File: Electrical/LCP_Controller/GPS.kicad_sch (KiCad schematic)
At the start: 12 parts, among them J12 SALEAE_TEST, J34 Conn_01x04, Q10 TSM500P02CX RFG, U13 MAX-M8Q

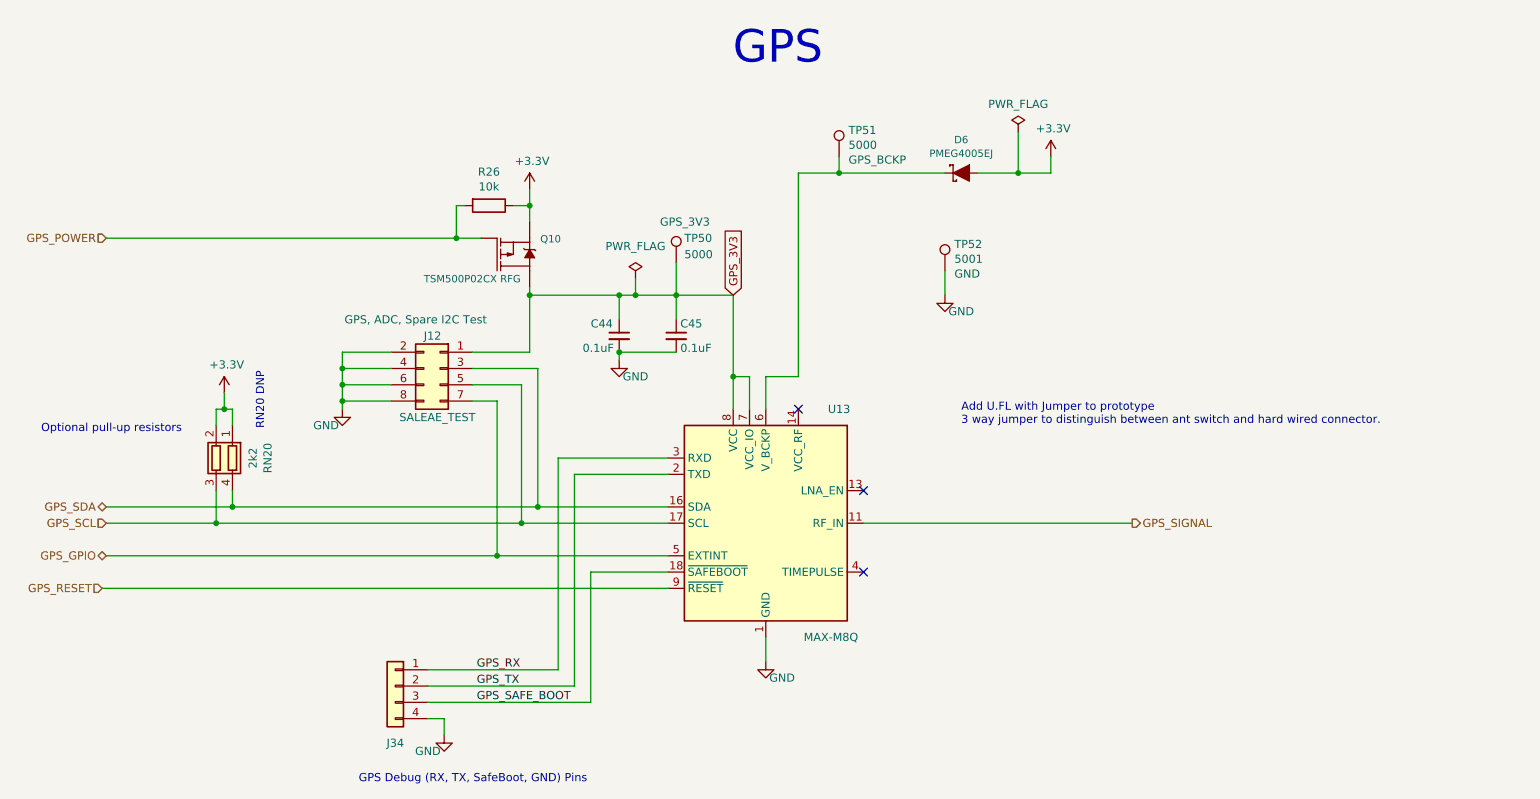
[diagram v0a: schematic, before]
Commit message: Hardware Revision : v0.3
1. modified schematic design, removed unnecessary test points.
2. pcb layout 2x8 Inches allowance dimension, layout is in progress
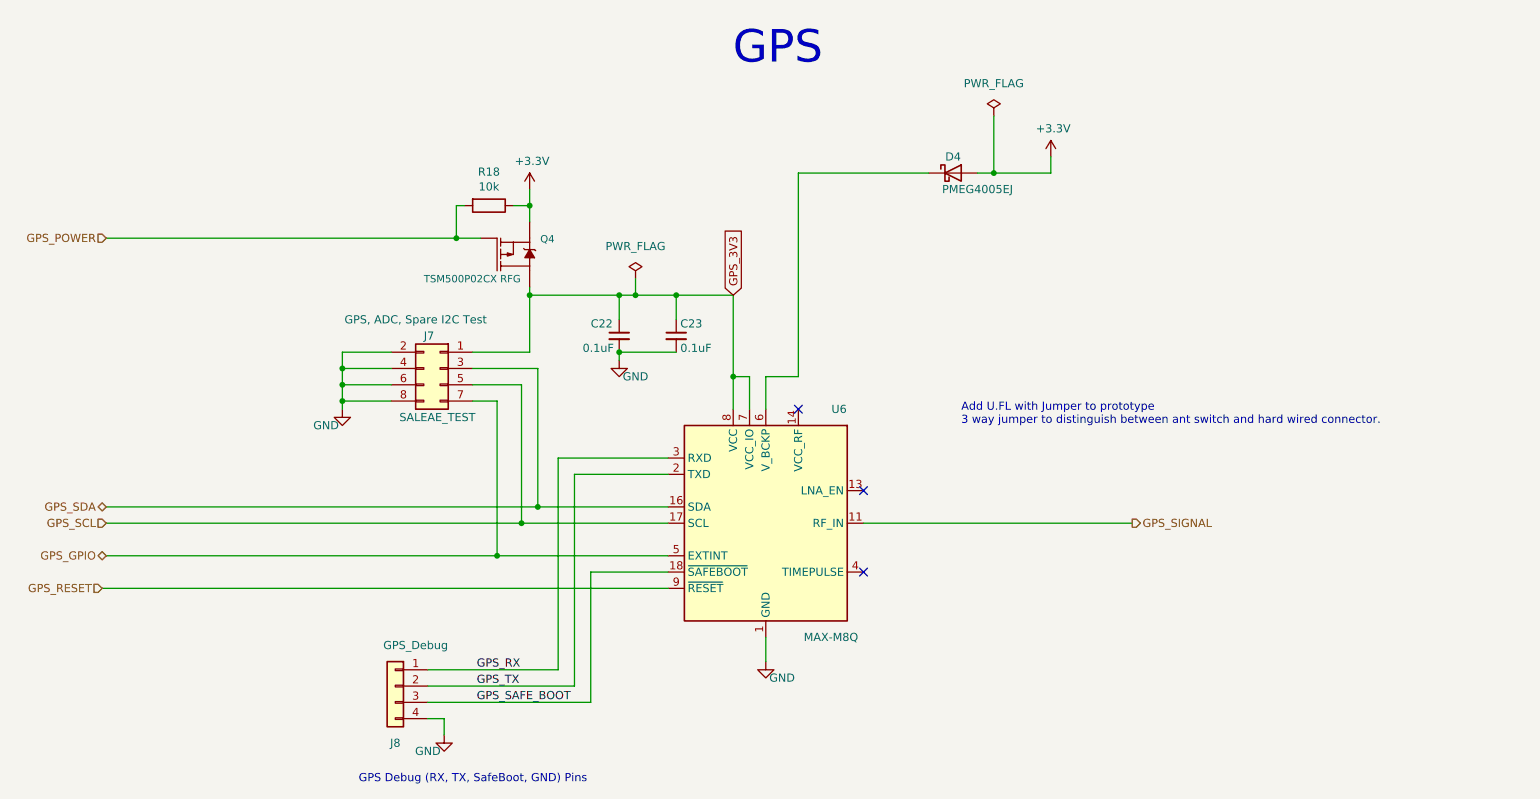
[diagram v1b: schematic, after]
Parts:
- removed D6: PMEG4005EJ, Diode_SMD:D_SOD-323F, symbol SparkFun-DiscreteSemi:DIODE-SCHOTTKY-PMEG4005EJ
- removed RN20: 2k2, Resistor_SMD:R_Array_Concave_2x0603, symbol Device:R_Pack02
- removed TP50, TP51: 5000, TestPoint:TestPoint_Keystone_5000-5004_Miniature, symbol Connector:TestPoint
- removed TP52: 5001, TestPoint:TestPoint_Keystone_5000-5004_Miniature, symbol Connector:TestPoint
- added D4: PMEG4005EJ, Diode_SMD:D_SOD-323, symbol Device:D_Schottky
- J8: renamed from J34; value Conn_01x04 -> GPS_Debug
- renumbered C44 to C22, C45 to C23, J12 to J7, Q10 to Q4, R26 to R18, U13 to U6
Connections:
- net +3.3V: now also D4.2 (A)
- net at U6.6 (V_BCKP): now also D4.1 (K)
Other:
- note removed: "Optional pull-up resistors"
- note removed: "RN20 DNP"

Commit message: Hw Rev : 0.3v
changed buck-coverter LMR50410XDBVR to BD9G102G-LB, added schotty diode.
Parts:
- D4: value PMEG4005EJ -> RB400VAM-50TR; MPN PMEG4005EJ -> RB400VAM-50TR
- U6: MPN (none) -> MAX-8C-0
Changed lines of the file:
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@@
+      (effects (font (size 1.27 1.27)) hide)
+    )
+    (property "MPN" "MAX-8C-0" (id 4) (at 161.29 106.68 0)
       (effects (font (size 1.27 1.27)) hide)
     )
@@
     (in_bom yes) (on_board yes)
     (property "Reference" "D4" (id 0) (at 190.5 49.53 0))
-    (property "Value" "PMEG4005EJ" (id 1) (at 194.31 54.61 0))
+    (property "Value" "RB400VAM-50TR" (id 1) (at 194.31 54.61 0))
     (property "Footprint" "Diode_SMD:D_SOD-323" (id 2) (at 190.5 52.07 0)
       (effects (font (size 1.27 1.27)) hide)
@@
       (effects (font (size 1.27 1.27)) hide)
     )
-    (property "MPN" "PMEG4005EJ" (id 4) (at 190.5 52.07 0)
+    (property "MPN" "RB400VAM-50TR" (id 4) (at 190.5 52.07 0)
       (effects (font (size 1.27 1.27)) hide)
     )

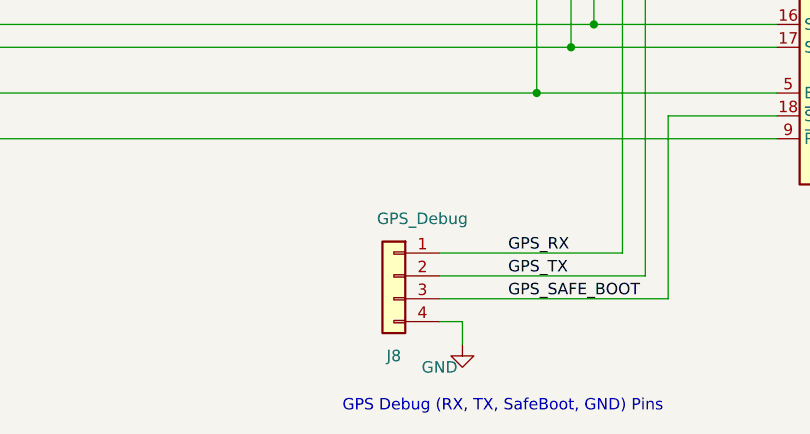
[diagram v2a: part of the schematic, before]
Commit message: Hw Rev : 0.3v updated
changed TRS3122ERGER to TRS3122ERGET due to shortage of part.
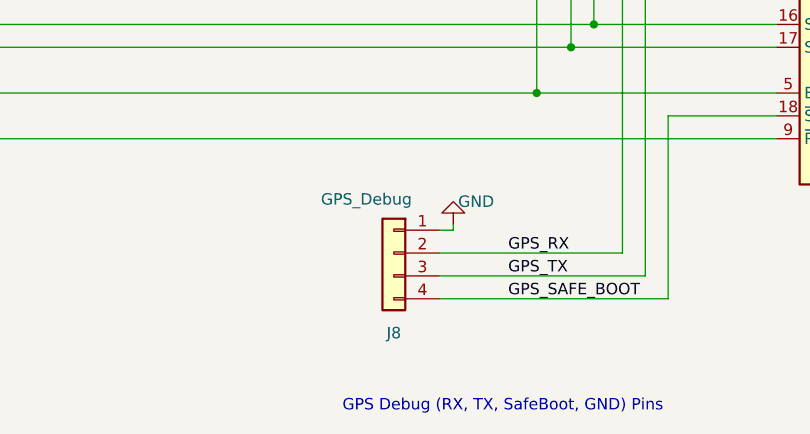
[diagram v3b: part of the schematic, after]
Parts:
- D4: footprint Diode_SMD:D_SOD-323 -> Diode_SMD:D_SOD-323F
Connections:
- net GND: now also J8.1 (Pin_1); no longer J8.4 (Pin_4)
- net GPS_RX: now also J8.2 (Pin_2); no longer J8.1 (Pin_1)
- net GPS_SAFE_BOOT: now also J8.4 (Pin_4); no longer J8.3 (Pin_3)
- net GPS_TX: now also J8.3 (Pin_3); no longer J8.2 (Pin_2)
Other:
- moved on the sheet: J8
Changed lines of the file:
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@@
-    (stroke (width 0) (type default) (color 0 0 0 0))
-  )
-  (wire (pts (xy 111.125 137.16) (xy 108.585 137.16))
     (stroke (width 0) (type default) (color 0 0 0 0))
   )
@@
     (stroke (width 0) (type default) (color 0 0 0 0))
   )
+  (wire (pts (xy 110.109 127) (xy 108.585 127))
+    (stroke (width 0) (type default) (color 0 0 0 0))
+  )
   (wire (pts (xy 113.03 57.15) (xy 114.3 57.15))
     (stroke (width 0) (type default) (color 0 0 0 0))
@@
     (stroke (width 0) (type default) (color 0 0 0 0))
   )
+  (wire (pts (xy 110.109 126.365) (xy 110.109 127))
+    (stroke (width 0) (type default) (color 0 0 0 0))
+  )
   (wire (pts (xy 146.05 96.52) (xy 128.905 96.52))
     (stroke (width 0) (type default) (color 0 0 0 0))
   )
   (wire (pts (xy 194.31 52.07) (xy 196.85 52.07))
-    (stroke (width 0) (type default) (color 0 0 0 0))
-  )
-  (wire (pts (xy 111.125 139.7) (xy 111.125 137.16))
     (stroke (width 0) (type default) (color 0 0 0 0))
   )
@@
     (property "Reference" "D4" (id 0) (at 190.5 49.53 0))
     (property "Value" "RB400VAM-50TR" (id 1) (at 194.31 54.61 0))
-    (property "Footprint" "Diode_SMD:D_SOD-323" (id 2) (at 190.5 52.07 0)
+    (property "Footprint" "Diode_SMD:D_SOD-323F" (id 2) (at 190.5 52.07 0)
       (effects (font (size 1.27 1.27)) hide)
     )
@@
     (pin "2")
   )
-  (symbol (lib_id "Connector_Generic:Conn_01x04") (at 103.505 132.08 0) (mirror y) (unit 1)
-    (in_bom yes) (on_board yes)
-    (property "Reference" "J8" (id 0) (at 103.505 140.97 0))
-    (property "Value" "GPS_Debug" (id 1) (at 106.68 125.73 0))
-    (property "Footprint" "Connector_PinHeader_2.54mm:PinHeader_1x04_P2.54mm_Vertical" (id 2) (at 103.505 132.08 0)
-      (effects (font (size 1.27 1.27)) hide)
-    )
-    (property "Datasheet" "~" (id 3) (at 103.505 132.08 0)
-      (effects (font (size 1.27 1.27)) hide)
-    )
-    (property "MPN" "" (id 4) (at 103.505 132.08 0)
+  (symbol (lib_id "Connector_Generic:Conn_01x04") (at 103.505 129.54 0) (mirror y) (unit 1)
+    (in_bom yes) (on_board yes)
+    (property "Reference" "J8" (id 0) (at 103.505 138.43 0))
+    (property "Value" "GPS_Debug" (id 1) (at 100.457 123.571 0))
+    (property "Footprint" "Connector_PinHeader_2.54mm:PinHeader_1x04_P2.54mm_Vertical" (id 2) (at 103.505 129.54 0)
+      (effects (font (size 1.27 1.27)) hide)
+    )
+    (property "Datasheet" "~" (id 3) (at 103.505 129.54 0)
+      (effects (font (size 1.27 1.27)) hide)
+    )
+    (property "MPN" "" (id 4) (at 103.505 129.54 0)
       (effects (font (size 1.27 1.27)) hide)
     )
@@
     (pin "4")
   )
-  (symbol (lib_id "power:GND") (at 111.125 139.7 0) (unit 1)
-    (in_bom yes) (on_board yes)
-    (property "Reference" "#PWR053" (id 0) (at 111.125 146.05 0)
-      (effects (font (size 1.27 1.27)) hide)
-    )
-    (property "Value" "GND" (id 1) (at 108.585 142.24 0))
-    (property "Footprint" "" (id 2) (at 111.125 139.7 0)
-      (effects (font (size 1.27 1.27)) hide)
-    )
-    (property "Datasheet" "" (id 3) (at 111.125 139.7 0)
-      (effects (font (size 1.27 1.27)) hide)
-    )
+  (symbol (lib_id "power:GND") (at 110.109 126.365 180) (unit 1)
+    (in_bom yes) (on_board yes)
+    (property "Reference" "#PWR053" (id 0) (at 110.109 120.015 0)
+      (effects (font (size 1.27 1.27)) hide)
+    )
+    (property "Value" "GND" (id 1) (at 112.649 123.825 0))
+    (property "Footprint" "" (id 2) (at 110.109 126.365 0)
+      (effects (font (size 1.27 1.27)) hide)
+    )
+    (property "Datasheet" "" (id 3) (at 110.109 126.365 0)
+      (effects (font (size 1.27 1.27)) hide)
+    )

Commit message: Hw Rev : 0.3v , update
changed package type D_SOD-323 to D_TUMD2 for D4,D7
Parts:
- D4: footprint Diode_SMD:D_SOD-323F -> Diode_SMD:D_TUMD2
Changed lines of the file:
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@@
     (property "Reference" "D4" (id 0) (at 190.5 49.53 0))
     (property "Value" "RB400VAM-50TR" (id 1) (at 194.31 54.61 0))
-    (property "Footprint" "Diode_SMD:D_SOD-323F" (id 2) (at 190.5 52.07 0)
+    (property "Footprint" "Diode_SMD:D_TUMD2" (id 2) (at 190.5 52.07 0)
       (effects (font (size 1.27 1.27)) hide)
     )

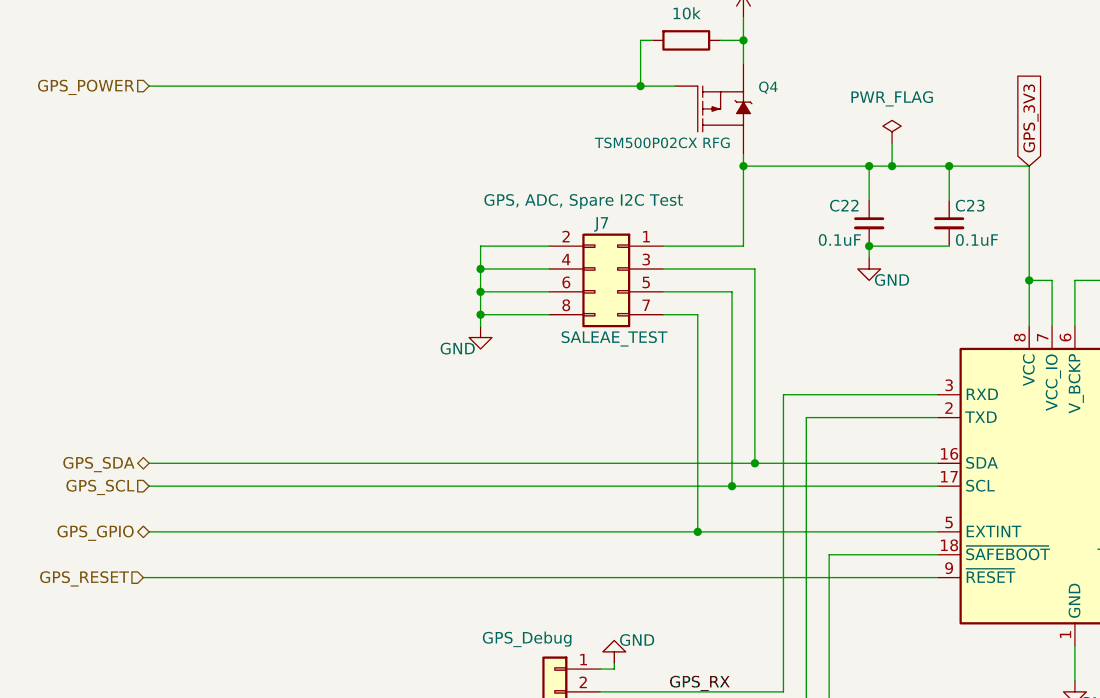
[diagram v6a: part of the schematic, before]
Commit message: New Layout
Changes for this Rev:
- Impedance Matched GPS traces
- Copper Pours
- Vias/Traces changed to bring down costs
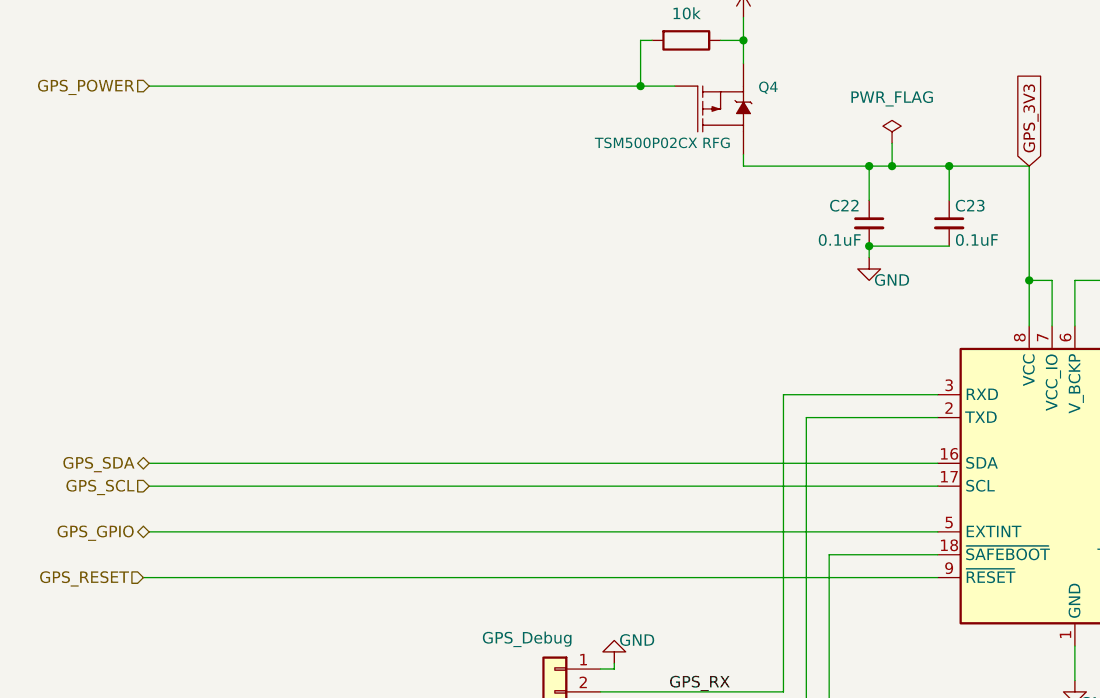
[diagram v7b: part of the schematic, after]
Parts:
- removed J7: SALEAE_TEST, Connector_PinHeader_2.54mm:PinHeader_2x04_P2.54mm_Vertical, symbol Connector_Generic:Conn_02x04_Odd_Even
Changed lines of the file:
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@@
     (comment 6 "Current Design Updated by: Joseph Kurina")
   )
-  (junction (at 119.38 111.76) (diameter 0) (color 0 0 0 0)
-  )
   (junction (at 140.97 71.12) (diameter 0) (color 0 0 0 0)
   )
-  (junction (at 95.25 87.63) (diameter 0) (color 0 0 0 0)
-  )
-  (junction (at 95.25 82.55) (diameter 0) (color 0 0 0 0)
-  )
   (junction (at 147.32 71.12) (diameter 0) (color 0 0 0 0)
-  )
-  (junction (at 125.73 104.14) (diameter 0) (color 0 0 0 0)
-  )
-  (junction (at 95.25 85.09) (diameter 0) (color 0 0 0 0)
-  )
-  (junction (at 124.46 71.12) (diameter 0) (color 0 0 0 0)
-  )
-  (junction (at 123.19 106.68) (diameter 0) (color 0 0 0 0)
   )
   (junction (at 138.43 71.12) (diameter 0) (color 0 0 0 0)
@@
     (stroke (width 0) (type default))
   )
-  (wire (pts (xy 119.38 87.63) (xy 119.38 111.76))
-    (stroke (width 0) (type default))
-  )
   (wire (pts (xy 138.43 80.01) (xy 147.32 80.01))
     (stroke (width 0) (type default))
   )
-  (wire (pts (xy 123.19 85.09) (xy 123.19 106.68))
-    (stroke (width 0) (type default))
-  )
   (wire (pts (xy 138.43 74.93) (xy 138.43 71.12))
     (stroke (width 0) (type default))
@@
     (stroke (width 0) (type default))
   )
-  (wire (pts (xy 58.42 106.68) (xy 123.19 106.68))
-    (stroke (width 0) (type default))
-  )
-  (wire (pts (xy 125.73 104.14) (xy 146.05 104.14))
+  (wire (pts (xy 58.42 104.14) (xy 146.05 104.14))
     (stroke (width 0) (type default))
   )
@@
     (stroke (width 0) (type default))
   )
-  (wire (pts (xy 95.25 82.55) (xy 95.25 85.09))
-    (stroke (width 0) (type default))
-  )
-  (wire (pts (xy 115.57 85.09) (xy 123.19 85.09))
-    (stroke (width 0) (type default))
-  )
-  (wire (pts (xy 102.87 85.09) (xy 95.25 85.09))
-    (stroke (width 0) (type default))
-  )
   (wire (pts (xy 147.32 74.93) (xy 147.32 71.12))
     (stroke (width 0) (type default))
@@
     (stroke (width 0) (type default))
   )
-  (wire (pts (xy 95.25 87.63) (xy 95.25 88.9))
-    (stroke (width 0) (type default))
-  )
-  (wire (pts (xy 115.57 80.01) (xy 124.46 80.01))
-    (stroke (width 0) (type default))
-  )
-  (wire (pts (xy 95.25 80.01) (xy 102.87 80.01))
-    (stroke (width 0) (type default))
-  )
-  (wire (pts (xy 102.87 82.55) (xy 95.25 82.55))
-    (stroke (width 0) (type default))
-  )
   (wire (pts (xy 156.21 71.12) (xy 156.21 83.82))
     (stroke (width 0) (type default))
@@
     (stroke (width 0) (type default))
   )
-  (wire (pts (xy 58.42 111.76) (xy 119.38 111.76))
-    (stroke (width 0) (type default))
-  )
   (wire (pts (xy 58.42 62.23) (xy 113.03 62.23))
     (stroke (width 0) (type default))
@@
     (stroke (width 0) (type default))
   )
-  (wire (pts (xy 115.57 82.55) (xy 125.73 82.55))
-    (stroke (width 0) (type default))
-  )
   (wire (pts (xy 116.84 62.23) (xy 113.03 62.23))
     (stroke (width 0) (type default))
   )
-  (wire (pts (xy 102.87 87.63) (xy 95.25 87.63))
-    (stroke (width 0) (type default))
-  )
   (wire (pts (xy 196.85 52.07) (xy 205.74 52.07))
     (stroke (width 0) (type default))
@@
     (stroke (width 0) (type default))
   )
-  (wire (pts (xy 119.38 111.76) (xy 146.05 111.76))
+  (wire (pts (xy 58.42 111.76) (xy 146.05 111.76))
     (stroke (width 0) (type default))
   )
@@
     (stroke (width 0) (type default))
   )
-  (wire (pts (xy 95.25 85.09) (xy 95.25 87.63))
-    (stroke (width 0) (type default))
-  )
   (wire (pts (xy 131.445 132.08) (xy 108.585 132.08))
     (stroke (width 0) (type default))
   )
-  (wire (pts (xy 95.25 82.55) (xy 95.25 80.01))
-    (stroke (width 0) (type default))
-  )
   (wire (pts (xy 133.985 134.62) (xy 108.585 134.62))
     (stroke (width 0) (type default))
@@
     (stroke (width 0) (type default))
   )
-  (wire (pts (xy 58.42 104.14) (xy 125.73 104.14))
-    (stroke (width 0) (type default))
-  )
   (wire (pts (xy 128.905 129.54) (xy 108.585 129.54))
     (stroke (width 0) (type default))
   )
-  (wire (pts (xy 115.57 87.63) (xy 119.38 87.63))
-    (stroke (width 0) (type default))
-  )
-  (wire (pts (xy 123.19 106.68) (xy 146.05 106.68))
+  (wire (pts (xy 58.42 106.68) (xy 146.05 106.68))
     (stroke (width 0) (type default))
   )
@@
   )
   (wire (pts (xy 158.75 83.82) (xy 158.75 88.9))
-    (stroke (width 0) (type default))
-  )
-  (wire (pts (xy 125.73 82.55) (xy 125.73 104.14))
-    (stroke (width 0) (type default))
-  )
-  (wire (pts (xy 124.46 71.12) (xy 124.46 80.01))
     (stroke (width 0) (type default))
   )
@@
     (effects (font (size 1.27 1.27)) (justify right))
   )
-  (symbol (lib_id "Connector_Generic:Conn_02x04_Odd_Even") (at 110.49 82.55 0) (mirror y) (unit 1)
-    (in_bom yes) (on_board yes) (dnp no)
-    (property "Reference" "J7" (at 107.95 77.47 0)
-      (effects (font (size 1.27 1.27)) (justify right))
-    )
-    (property "Value" "SALEAE_TEST" (at 104.14 90.17 0)
-      (effects (font (size 1.27 1.27)) (justify right))
-    )
-    (property "Footprint" "Connector_PinHeader_2.54mm:PinHeader_2x04_P2.54mm_Vertical" (at 110.49 82.55 0)
-      (effects (font (size 1.27 1.27)) hide)
-    )
-    (property "Datasheet" "~" (at 110.49 82.55 0)
-      (effects (font (size 1.27 1.27)) hide)
-    )
-    (property "TestPoint" "GPS, ADC, Spare I2C Test" (at 106.68 74.93 0)
-      (effects (font (size 1.27 1.27)))
-    )
-    (property "MPN" "0010897080" (at 110.49 82.55 0)
-      (effects (font (size 1.27 1.27)) hide)
-    )
-    (pin "1")
-    (pin "2")
-    (pin "3")
-    (pin "4")
-    (pin "5")
-    (pin "6")
-    (pin "7")
-    (pin "8")
-    (instances
-      (project "LCP_Controller"
-        (path "/df0f358a-57ab-4ee9-8b36-6ce64ef9d813/00000000-0000-0000-0000-00005edb3949"
-          (reference "J7") (unit 1)
-        )
-      )
-    )
-  )
-  (symbol (lib_id "power:GND") (at 95.25 88.9 0) (unit 1)
-    (in_bom yes) (on_board yes) (dnp no)
-    (property "Reference" "#PWR051" (at 95.25 95.25 0)
-      (effects (font (size 1.27 1.27)) hide)
-    )
-    (property "Value" "GND" (at 92.71 91.44 0)
-      (effects (font (size 1.27 1.27)))
-    )
-    (property "Footprint" "" (at 95.25 88.9 0)
-      (effects (font (size 1.27 1.27)) hide)
-    )
-    (property "Datasheet" "" (at 95.25 88.9 0)
-      (effects (font (size 1.27 1.27)) hide)
-    )
-    (pin "1")
-    (instances
-      (project "LCP_Controller"
-        (path "/df0f358a-57ab-4ee9-8b36-6ce64ef9d813/00000000-0000-0000-0000-00005edb3949"
-          (reference "#PWR051") (unit 1)
-        )
-      )
-    )
-  )
   (symbol (lib_id "Device:R") (at 118.11 57.15 270) (unit 1)
